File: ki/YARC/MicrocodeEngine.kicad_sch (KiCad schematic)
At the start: 12 parts

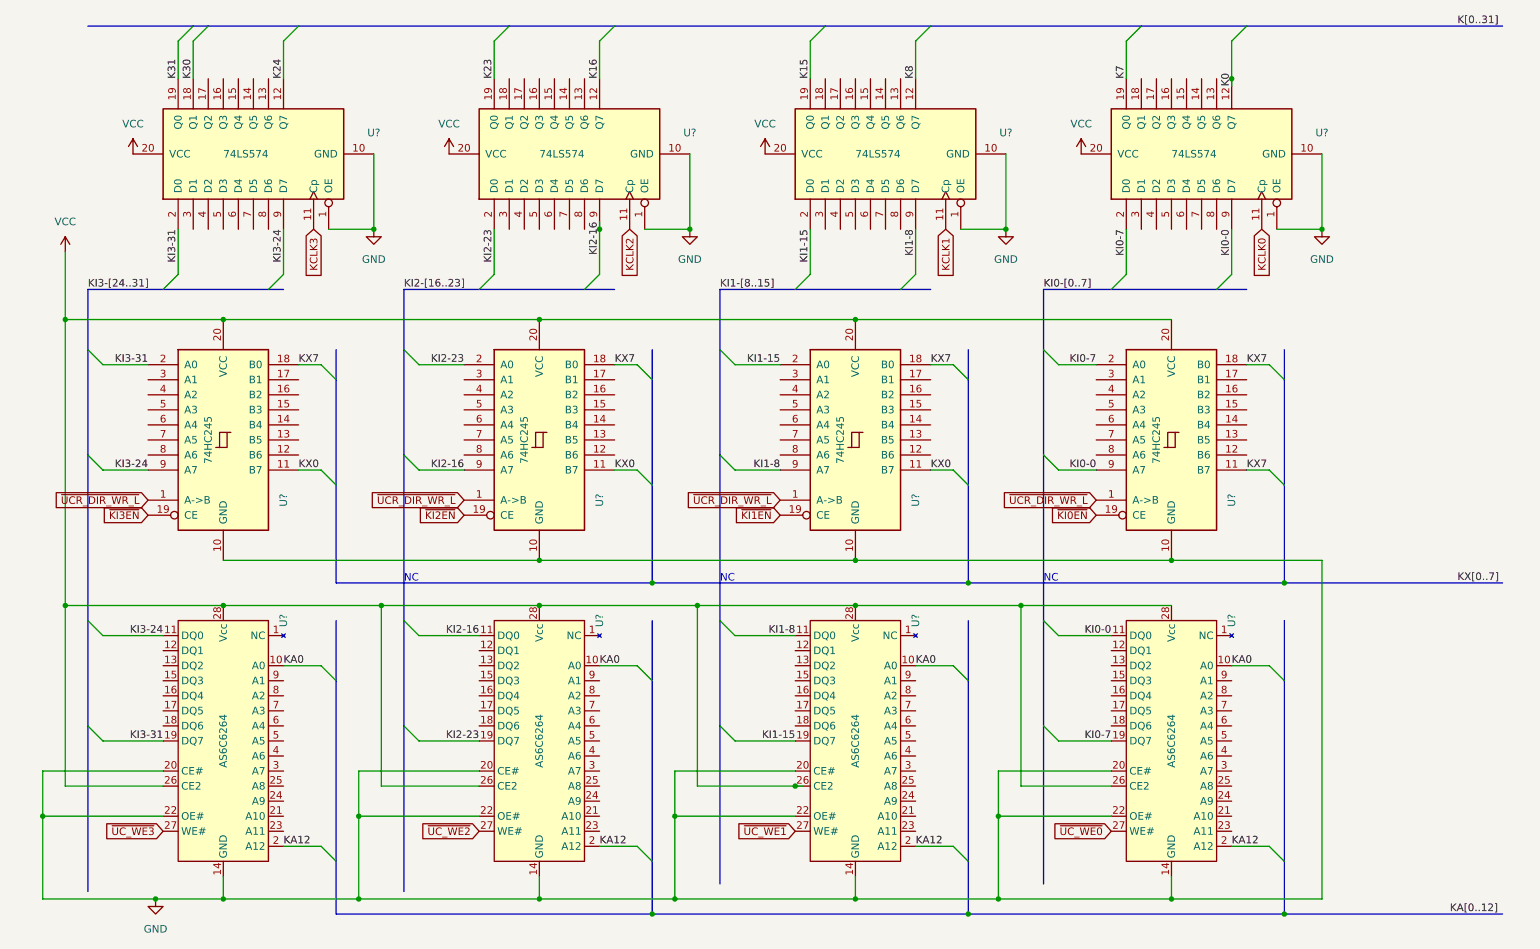
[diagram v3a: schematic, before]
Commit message: Assign part labels (U-numbers) in KiCad and start adding them to Fritzing layouts
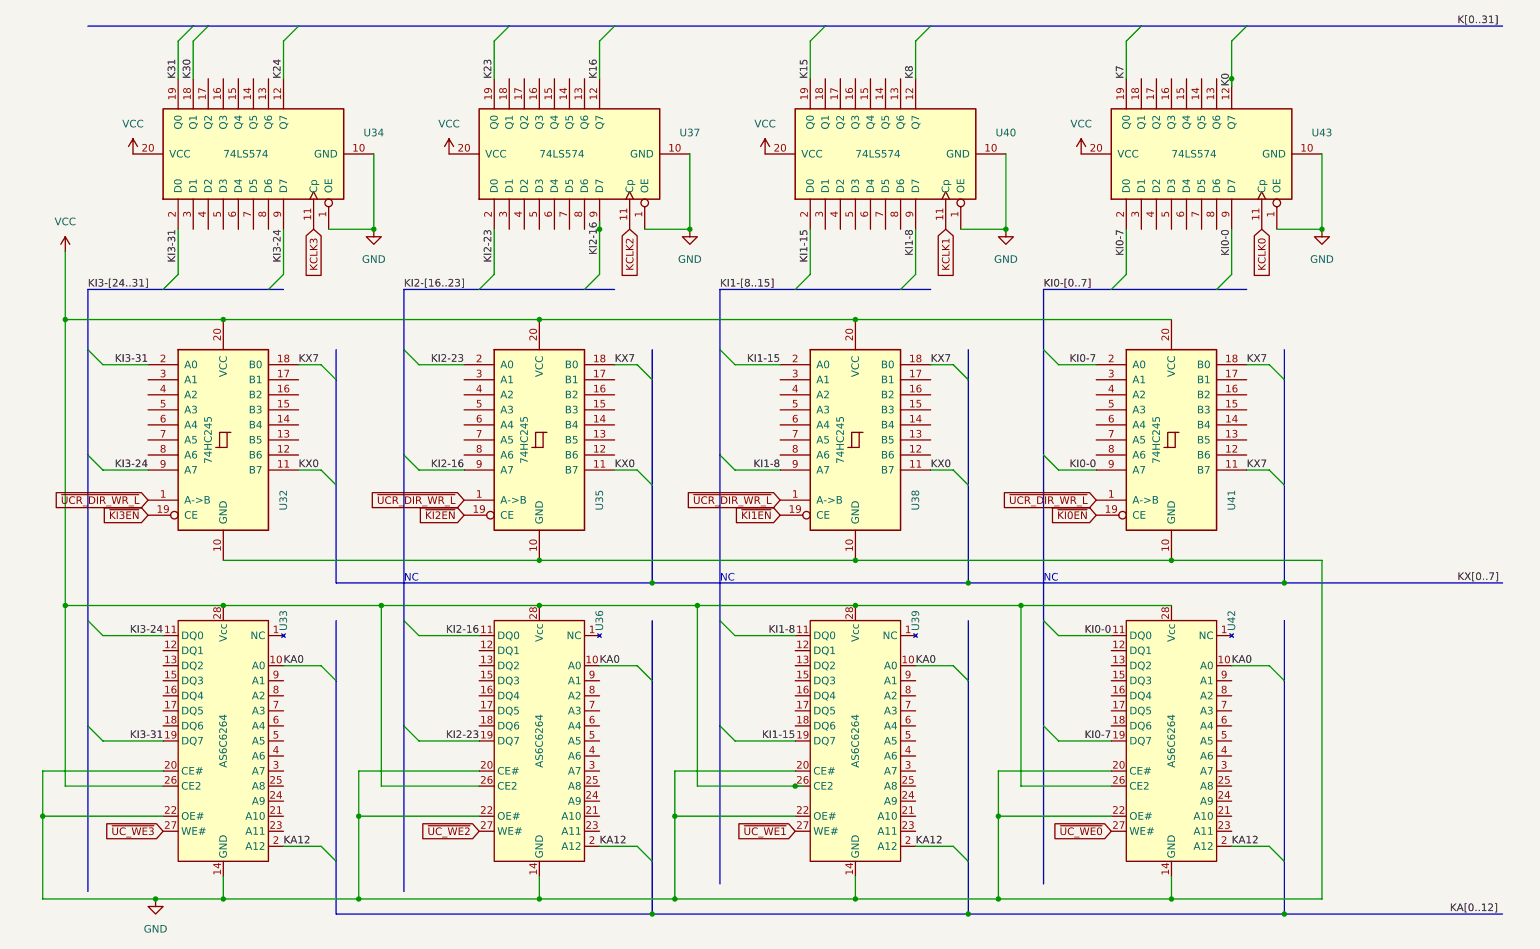
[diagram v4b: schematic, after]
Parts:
- gave numbers to parts that had none: 12
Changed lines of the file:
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@@
   (symbol (lib_id "74xx:74LS574") (at 104.14 39.37 90) (unit 1)
     (in_bom yes) (on_board yes)
-    (property "Reference" "U?" (id 0) (at 124.46 35.7886 90))
+    (property "Reference" "U37" (id 0) (at 124.46 35.7886 90))
     (property "Value" "74LS574" (id 1) (at 102.87 39.37 90))
     (property "Footprint" "" (id 2) (at 104.14 39.37 0)
@@
   (symbol (lib_id "power:GND") (at 71.12 52.07 0) (unit 1)
     (in_bom yes) (on_board yes) (fields_autoplaced)
-    (property "Reference" "#PWR?" (id 0) (at 71.12 58.42 0)
+    (property "Reference" "#PWR027" (id 0) (at 71.12 58.42 0)
       (effects (font (size 1.27 1.27)) hide)
     )
@@
   (symbol (lib_id "pdxjjb:AS6C6264") (at 99.06 143.51 0) (mirror y) (unit 1)
     (in_bom yes) (on_board yes)
-    (property "Reference" "U?" (id 0) (at 109.22 118.11 90))
+    (property "Reference" "U36" (id 0) (at 109.22 118.11 90))
     (property "Value" "AS6C6264" (id 1) (at 99.06 138.43 90))
     (property "Footprint" "" (id 2) (at 120.65 114.3 0)
@@
   (symbol (lib_id "power:VCC") (at 30.48 39.37 0) (unit 1)
     (in_bom yes) (on_board yes)
-    (property "Reference" "#PWR?" (id 0) (at 30.48 43.18 0)
+    (property "Reference" "#PWR016" (id 0) (at 30.48 43.18 0)
       (effects (font (size 1.27 1.27)) hide)
     )
@@
   (symbol (lib_id "power:GND") (at 124.46 52.07 0) (unit 1)
     (in_bom yes) (on_board yes) (fields_autoplaced)
-    (property "Reference" "#PWR?" (id 0) (at 124.46 58.42 0)
+    (property "Reference" "#PWR033" (id 0) (at 124.46 58.42 0)
       (effects (font (size 1.27 1.27)) hide)
     )
@@
   (symbol (lib_id "74xx:74HC245") (at 45.72 87.63 0) (unit 1)
     (in_bom yes) (on_board yes)
-    (property "Reference" "U?" (id 0) (at 55.88 97.79 90))
+    (property "Reference" "U32" (id 0) (at 55.88 97.79 90))
     (property "Value" "74HC245" (id 1) (at 43.18 87.63 90))
     (property "Footprint" "" (id 2) (at 45.72 87.63 0)
@@
   (symbol (lib_id "74xx:74LS574") (at 210.82 39.37 90) (unit 1)
     (in_bom yes) (on_board yes)
-    (property "Reference" "U?" (id 0) (at 231.14 35.7886 90))
+    (property "Reference" "U43" (id 0) (at 231.14 35.7886 90))
     (property "Value" "74LS574" (id 1) (at 209.55 39.37 90))
     (property "Footprint" "" (id 2) (at 210.82 39.37 0)
@@
   (symbol (lib_id "power:VCC") (at 190.5 39.37 0) (unit 1)
     (in_bom yes) (on_board yes)
-    (property "Reference" "#PWR?" (id 0) (at 190.5 43.18 0)
+    (property "Reference" "#PWR043" (id 0) (at 190.5 43.18 0)
       (effects (font (size 1.27 1.27)) hide)
     )
@@
   (symbol (lib_id "power:GND") (at 34.29 165.1 0) (unit 1)
     (in_bom yes) (on_board yes) (fields_autoplaced)
-    (property "Reference" "#PWR?" (id 0) (at 34.29 171.45 0)
+    (property "Reference" "#PWR017" (id 0) (at 34.29 171.45 0)
       (effects (font (size 1.27 1.27)) hide)
     )
@@
   (symbol (lib_id "power:GND") (at 231.14 52.07 0) (unit 1)
     (in_bom yes) (on_board yes) (fields_autoplaced)
-    (property "Reference" "#PWR?" (id 0) (at 231.14 58.42 0)
+    (property "Reference" "#PWR044" (id 0) (at 231.14 58.42 0)
       (effects (font (size 1.27 1.27)) hide)
     )
@@
   (symbol (lib_id "pdxjjb:AS6C6264") (at 45.72 143.51 0) (mirror y) (unit 1)
     (in_bom yes) (on_board yes)
-    (property "Reference" "U?" (id 0) (at 55.88 118.11 90))
+    (property "Reference" "U33" (id 0) (at 55.88 118.11 90))
     (property "Value" "AS6C6264" (id 1) (at 45.72 138.43 90))
     (property "Footprint" "" (id 2) (at 67.31 114.3 0)
@@
   (symbol (lib_id "74xx:74LS574") (at 50.8 39.37 90) (unit 1)
     (in_bom yes) (on_board yes)
-    (property "Reference" "U?" (id 0) (at 71.12 35.7886 90))
+    (property "Reference" "U34" (id 0) (at 71.12 35.7886 90))
     (property "Value" "74LS574" (id 1) (at 49.53 39.37 90))
     (property "Footprint" "" (id 2) (at 50.8 39.37 0)
@@
   (symbol (lib_id "74xx:74LS574") (at 157.48 39.37 90) (unit 1)
     (in_bom yes) (on_board yes)
-    (property "Reference" "U?" (id 0) (at 177.8 35.7886 90))
+    (property "Reference" "U40" (id 0) (at 177.8 35.7886 90))
     (property "Value" "74LS574" (id 1) (at 156.21 39.37 90))
     (property "Footprint" "" (id 2) (at 157.48 39.37 0)
@@
   (symbol (lib_id "pdxjjb:AS6C6264") (at 152.4 143.51 0) (mirror y) (unit 1)
     (in_bom yes) (on_board yes)
-    (property "Reference" "U?" (id 0) (at 162.56 118.11 90))
+    (property "Reference" "U39" (id 0) (at 162.56 118.11 90))
     (property "Value" "AS6C6264" (id 1) (at 152.4 138.43 90))
     (property "Footprint" "" (id 2) (at 173.99 114.3 0)
@@
   (symbol (lib_id "74xx:74HC245") (at 99.06 87.63 0) (unit 1)
     (in_bom yes) (on_board yes)
-    (property "Reference" "U?" (id 0) (at 109.22 97.79 90))
+    (property "Reference" "U35" (id 0) (at 109.22 97.79 90))
     (property "Value" "74HC245" (id 1) (at 96.52 87.63 90))
     (property "Footprint" "" (id 2) (at 99.06 87.63 0)
@@
   (symbol (lib_id "74xx:74HC245") (at 205.74 87.63 0) (unit 1)
     (in_bom yes) (on_board yes)
-    (property "Reference" "U?" (id 0) (at 215.9 97.79 90))
+    (property "Reference" "U41" (id 0) (at 215.9 97.79 90))
     (property "Value" "74HC245" (id 1) (at 203.2 87.63 90))
     (property "Footprint" "" (id 2) (at 205.74 87.63 0)
@@
   (symbol (lib_id "power:VCC") (at 83.82 39.37 0) (unit 1)
     (in_bom yes) (on_board yes)
-    (property "Reference" "#PWR?" (id 0) (at 83.82 43.18 0)
+    (property "Reference" "#PWR032" (id 0) (at 83.82 43.18 0)
       (effects (font (size 1.27 1.27)) hide)
     )
@@
   (symbol (lib_id "power:VCC") (at 137.16 39.37 0) (unit 1)
     (in_bom yes) (on_board yes)
-    (property "Reference" "#PWR?" (id 0) (at 137.16 43.18 0)
+    (property "Reference" "#PWR039" (id 0) (at 137.16 43.18 0)
       (effects (font (size 1.27 1.27)) hide)
     )
@@
   (symbol (lib_id "power:VCC") (at 19.05 55.88 0) (unit 1)
     (in_bom yes) (on_board yes)
-    (property "Reference" "#PWR?" (id 0) (at 19.05 59.69 0)
+    (property "Reference" "#PWR015" (id 0) (at 19.05 59.69 0)
       (effects (font (size 1.27 1.27)) hide)
     )
@@
   (symbol (lib_id "power:GND") (at 177.8 52.07 0) (unit 1)
     (in_bom yes) (on_board yes) (fields_autoplaced)
-    (property "Reference" "#PWR?" (id 0) (at 177.8 58.42 0)
+    (property "Reference" "#PWR041" (id 0) (at 177.8 58.42 0)
       (effects (font (size 1.27 1.27)) hide)
     )
@@
   (symbol (lib_id "pdxjjb:AS6C6264") (at 205.74 143.51 0) (mirror y) (unit 1)
     (in_bom yes) (on_board yes)
-    (property "Reference" "U?" (id 0) (at 215.9 118.11 90))
+    (property "Reference" "U42" (id 0) (at 215.9 118.11 90))
     (property "Value" "AS6C6264" (id 1) (at 205.74 138.43 90))
     (property "Footprint" "" (id 2) (at 227.33 114.3 0)
@@
   (symbol (lib_id "74xx:74HC245") (at 152.4 87.63 0) (unit 1)
     (in_bom yes) (on_board yes)
-    (property "Reference" "U?" (id 0) (at 162.56 97.79 90))
+    (property "Reference" "U38" (id 0) (at 162.56 97.79 90))
     (property "Value" "74HC245" (id 1) (at 149.86 87.63 90))
     (property "Footprint" "" (id 2) (at 152.4 87.63 0)

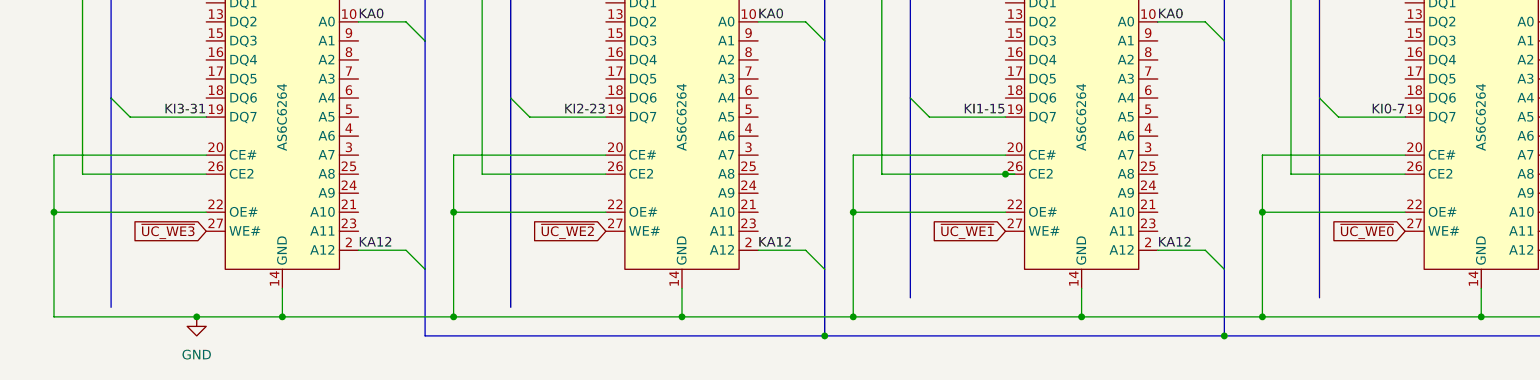
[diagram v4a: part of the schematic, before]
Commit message: Fix - add microcode RAM enables to schematic
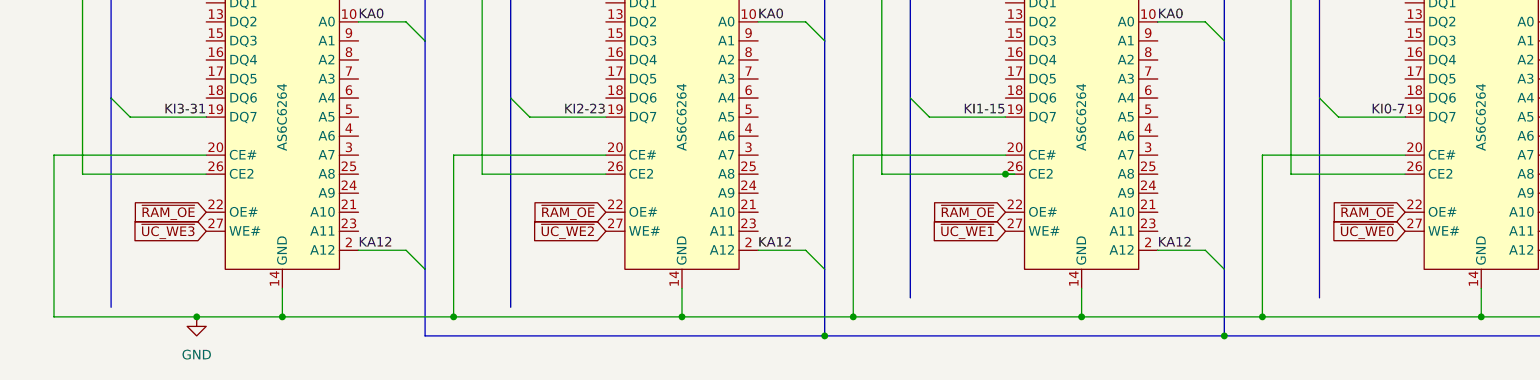
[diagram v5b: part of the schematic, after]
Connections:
- net GND: no longer U33.22 (OE#), U36.22 (OE#), U39.22 (OE#), U42.22 (OE#)
- new net ~{RAM_OE}: U33.22 (OE#), U36.22 (OE#), U39.22 (OE#), U42.22 (OE#)
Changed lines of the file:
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@@
   (junction (at 68.58 165.1) (diameter 0) (color 0 0 0 0)
   )
-  (junction (at 68.58 151.13) (diameter 0) (color 0 0 0 0)
-  )
   (junction (at 224.79 111.76) (diameter 0) (color 0 0 0 0)
   )
@@
   (junction (at 215.9 26.67) (diameter 0) (color 0 0 0 0)
   )
-  (junction (at 15.24 151.13) (diameter 0) (color 0 0 0 0)
-  )
   (junction (at 205.74 107.95) (diameter 0) (color 0 0 0 0)
   )
@@
   (junction (at 45.72 67.31) (diameter 0) (color 0 0 0 0)
   )
-  (junction (at 176.53 151.13) (diameter 0) (color 0 0 0 0)
-  )
   (junction (at 118.11 111.76) (diameter 0) (color 0 0 0 0)
   )
@@
   (junction (at 19.05 115.57) (diameter 0) (color 0 0 0 0)
   )
-  (junction (at 121.92 151.13) (diameter 0) (color 0 0 0 0)
-  )
   (junction (at 180.34 115.57) (diameter 0) (color 0 0 0 0)
   )
@@
     (stroke (width 0) (type default) (color 0 0 0 0))
   )
-  (wire (pts (xy 15.24 165.1) (xy 15.24 151.13))
+  (wire (pts (xy 15.24 143.51) (xy 15.24 165.1))
     (stroke (width 0) (type default) (color 0 0 0 0))
   )
@@
     (stroke (width 0) (type default) (color 0 0 0 0))
   )
-  (wire (pts (xy 121.92 151.13) (xy 121.92 165.1))
-    (stroke (width 0) (type default) (color 0 0 0 0))
-  )
   (wire (pts (xy 25.4 138.43) (xy 35.56 138.43))
     (stroke (width 0) (type default) (color 0 0 0 0))
@@
     (stroke (width 0) (type default) (color 0 0 0 0))
   )
-  (wire (pts (xy 176.53 151.13) (xy 176.53 165.1))
+  (wire (pts (xy 176.53 143.51) (xy 176.53 165.1))
     (stroke (width 0) (type default) (color 0 0 0 0))
   )
@@
     (stroke (width 0) (type default) (color 0 0 0 0))
   )
-  (wire (pts (xy 176.53 143.51) (xy 176.53 151.13))
-    (stroke (width 0) (type default) (color 0 0 0 0))
-  )
   (wire (pts (xy 109.22 20.32) (xy 109.22 26.67))
     (stroke (width 0) (type default) (color 0 0 0 0))
@@
     (stroke (width 0) (type default) (color 0 0 0 0))
   )
-  (wire (pts (xy 88.9 151.13) (xy 68.58 151.13))
-    (stroke (width 0) (type default) (color 0 0 0 0))
-  )
   (wire (pts (xy 78.74 92.71) (xy 86.36 92.71))
     (stroke (width 0) (type default) (color 0 0 0 0))
@@
     (stroke (width 0) (type default) (color 0 0 0 0))
   )
-  (wire (pts (xy 121.92 143.51) (xy 121.92 151.13))
+  (wire (pts (xy 121.92 143.51) (xy 121.92 165.1))
     (stroke (width 0) (type default) (color 0 0 0 0))
   )
@@
     (stroke (width 0) (type default) (color 0 0 0 0))
   )
-  (wire (pts (xy 68.58 143.51) (xy 68.58 151.13))
-    (stroke (width 0) (type default) (color 0 0 0 0))
-  )
   (wire (pts (xy 186.69 74.93) (xy 193.04 74.93))
     (stroke (width 0) (type default) (color 0 0 0 0))
@@
     (stroke (width 0) (type default) (color 0 0 0 0))
   )
-  (wire (pts (xy 15.24 151.13) (xy 35.56 151.13))
-    (stroke (width 0) (type default) (color 0 0 0 0))
-  )
   (wire (pts (xy 186.69 92.71) (xy 193.04 92.71))
     (stroke (width 0) (type default) (color 0 0 0 0))
@@
     (stroke (width 0) (type default) (color 0 0 0 0))
   )
-  (wire (pts (xy 68.58 151.13) (xy 68.58 165.1))
+  (wire (pts (xy 68.58 143.51) (xy 68.58 165.1))
     (stroke (width 0) (type default) (color 0 0 0 0))
   )
@@
     (stroke (width 0) (type default) (color 0 0 0 0))
   )
-  (wire (pts (xy 142.24 151.13) (xy 121.92 151.13))
-    (stroke (width 0) (type default) (color 0 0 0 0))
-  )
   (wire (pts (xy 45.72 165.1) (xy 34.29 165.1))
     (stroke (width 0) (type default) (color 0 0 0 0))
@@
     (stroke (width 0) (type default) (color 0 0 0 0))
   )
-  (wire (pts (xy 195.58 151.13) (xy 176.53 151.13))
-    (stroke (width 0) (type default) (color 0 0 0 0))
-  )
   (bus (pts (xy 171.45 167.64) (xy 224.79 167.64))
-    (stroke (width 0) (type default) (color 0 0 0 0))
-  )
-  (wire (pts (xy 15.24 143.51) (xy 15.24 151.13))
     (stroke (width 0) (type default) (color 0 0 0 0))
   )
@@
     )
   )
+  (global_label "~{RAM_OE}" (shape input) (at 35.56 151.13 180) (fields_autoplaced)
+    (effects (font (size 1.27 1.27)) (justify right))
+    (property "Intersheet References" "${INTERSHEET_REFS}" (id 0) (at 25.8898 151.0506 0)
+      (effects (font (size 1.27 1.27)) (justify right) hide)
+    )
+  )
+  (global_label "~{RAM_OE}" (shape input) (at 88.9 151.13 180) (fields_autoplaced)
+    (effects (font (size 1.27 1.27)) (justify right))
+    (property "Intersheet References" "${INTERSHEET_REFS}" (id 0) (at 79.2298 151.0506 0)
+      (effects (font (size 1.27 1.27)) (justify right) hide)
+    )
+  )
   (global_label "~{UCR_DIR_WR_L}" (shape input) (at 139.7 97.79 180) (fields_autoplaced)
     (effects (font (size 1.27 1.27)) (justify right))
@@
       (effects (font (size 1.27 1.27)) (justify right) hide)
     )
+  )
+  (global_label "~{RAM_OE}" (shape input) (at 142.24 151.13 180) (fields_autoplaced)
+    (effects (font (size 1.27 1.27)) (justify right))
+    (property "Intersheet References" "${INTERSHEET_REFS}" (id 0) (at 132.5698 151.0506 0)
+      (effects (font (size 1.27 1.27)) (justify right) hide)
+    )
+  )
+  (global_label "~{RAM_OE}" (shape input) (at 195.58 151.13 180) (fields_autoplaced)
+    (effects (font (size 1.27 1.27)) (justify right))
+    (property "Intersheet References" "${INTERSHEET_REFS}" (id 0) (at 185.9098 151.0506 0)
+      (effects (font (size 1.27 1.27)) (justify right) hide)
+    )
